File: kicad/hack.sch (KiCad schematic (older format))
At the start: 34 parts, among them P1 USB_micro, P2 CONN_01X13, P3 CONN_01X13, P4 CONN_01X01, U1 MIC5528, U2 STF202, U3 ATSAMD21E, X1 ABS07

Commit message: Added VBUS pin, GND pin near VDDANA
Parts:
- added P5, P6: CONN_01X01, hack-footprints:Pin_Castellated_1x01, symbol CONN_01X01
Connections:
- net GND: now also P6.1 (P1)
- net VBUS: now also P5.1 (P1)
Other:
- moved on the sheet: P4
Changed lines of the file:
@@
 Text GLabel 2825 6075 2    40   BiDi ~ 0
 PA16/6
-Text GLabel 2425 7275 3    40   Output ~ 0
+Text GLabel 2625 7275 3    40   Output ~ 0
 VDDANA
 $Comp
@@
 L CONN_01X01 P4
 U 1 1 568E26C4
-P 2425 7075
-F 0 "P4" V 2425 7175 40  0000 L CNB
-F 1 "CONN_01X01" V 2525 6900 40  0000 L CNB
-F 2 "hack-footprints:Pin_Castellated_1x01" H 2425 7075 50  0001 C CNN
-F 3 "" H 2425 7075 50  0000 C CNN
-	1    2425 7075
+P 2625 7075
+F 0 "P4" V 2625 7175 40  0000 L CNB
+F 1 "CONN_01X01" V 2725 6900 40  0000 L CNB
+F 2 "hack-footprints:Pin_Castellated_1x01" H 2625 7075 50  0001 C CNN
+F 3 "" H 2625 7075 50  0000 C CNN
+	1    2625 7075
 	0    -1   -1   0
 $EndComp
@@
 	1    0    0    -1
 $EndComp
+Text GLabel 2225 7275 3    40   Output ~ 0
+VBUS
+$Comp
+L CONN_01X01 P5
+U 1 1 569F6050
+P 2225 7075
+F 0 "P5" V 2225 7175 40  0000 L CNB
+F 1 "CONN_01X01" V 2325 6900 40  0000 L CNB
+F 2 "hack-footprints:Pin_Castellated_1x01" H 2225 7075 50  0001 C CNN
+F 3 "" H 2225 7075 50  0000 C CNN
+	1    2225 7075
+	0    -1   -1   0
+$EndComp
+Text GLabel 1825 7275 3    40   Output ~ 0
+GND
+$Comp
+L CONN_01X01 P6
+U 1 1 569F8542
+P 1825 7075
+F 0 "P6" V 1825 7175 40  0000 L CNB
+F 1 "CONN_01X01" V 1925 6900 40  0000 L CNB
+F 2 "hack-footprints:Pin_Castellated_1x01" H 1825 7075 50  0001 C CNN
+F 3 "" H 1825 7075 50  0000 C CNN
+	1    1825 7075
+	0    -1   -1   0
+$EndComp
 $EndSCHEMATC

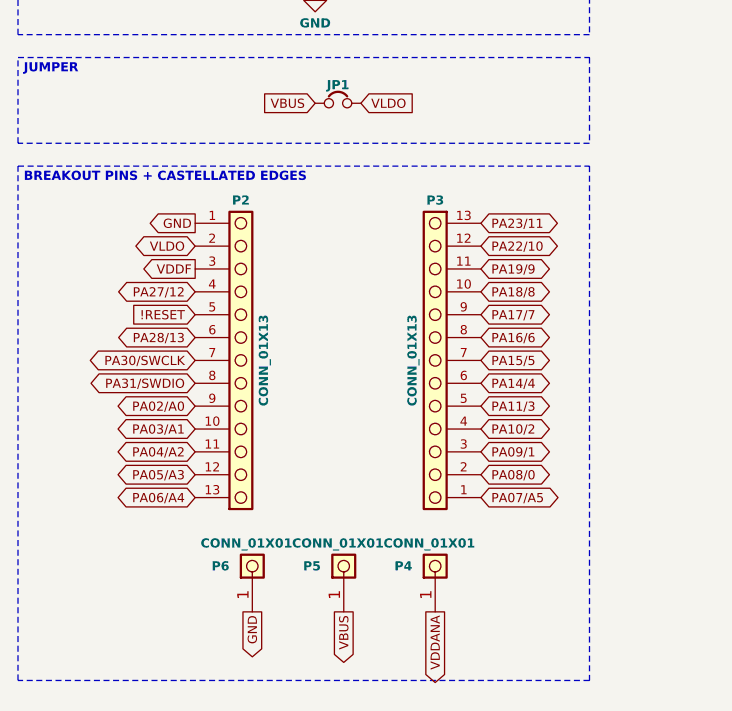
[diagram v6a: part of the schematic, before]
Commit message: Reducing board size (w.i.p.)
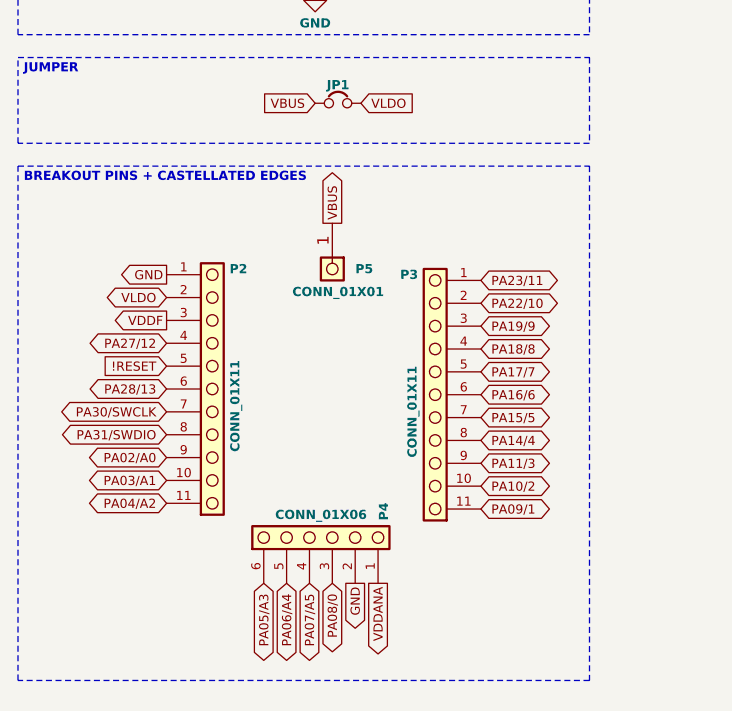
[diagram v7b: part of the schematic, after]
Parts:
- removed P2, P3: CONN_01X13, hack-footprints:Pin_Castellated_1x13, symbol CONN_01X13
- removed P4, P6: CONN_01X01, hack-footprints:Pin_Castellated_1x01, symbol CONN_01X01
- added P2, P3: CONN_01X11, hack-footprints:Pin_Castellated_1x11, symbol CONN_01X11
- added P4: CONN_01X06, hack-footprints:Pin_Castellated_1x06, symbol CONN_01X06
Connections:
- net !RESET: now also P2.5 (P5)
- net GND: now also P2.1 (P1), P4.2 (P2)
- net PA02/A0: now also P2.9 (P9)
- net PA03/A1: now also P2.10 (P10)
- net PA04/A2: now also P2.11 (P11)
- net PA05/A3: now also P4.6 (P6)
- net PA06/A4: now also P4.5 (P5)
- net PA07/A5: now also P4.4 (P4)
- net PA08/0: now also P4.3 (P3)
- net PA09/1: now also P3.11 (P11)
- net PA10/2: now also P3.10 (P10)
- net PA11/3: now also P3.9 (P9)
- net PA14/4: now also P3.8 (P8)
- net PA15/5: now also P3.7 (P7)
- net PA16/6: now also P3.6 (P6)
- net PA17/7: now also P3.5 (P5)
- net PA18/8: now also P3.4 (P4)
- net PA19/9: now also P3.3 (P3)
- net PA22/10: now also P3.2 (P2)
- net PA23/11: now also P3.1 (P1)
- net PA27/12: now also P2.4 (P4)
- net PA28/13: now also P2.6 (P6)
- net PA30/SWCLK: now also P2.7 (P7)
- net PA31/SWDIO: now also P2.8 (P8)
- net VDDANA: now also P4.1 (P1)
- net VDDF: now also P2.3 (P3)
- net VLDO: now also P2.2 (P2)
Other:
- moved on the sheet: P5
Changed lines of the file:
@@
-$EndComp
-$Comp
-L CONN_01X13 P2
-U 1 1 56587624
-P 1775 6175
-F 0 "P2" H 1775 6875 40  0000 C CNB
-F 1 "CONN_01X13" V 1875 6175 40  0000 C CNB
-F 2 "hack-footprints:Pin_Castellated_1x13" H 1775 6175 40  0001 C CNB
-F 3 "https://github.com/MickMad/HACK/tree/master/kicad/datasheets/xRxCzzzSxxN-RC_ST_11635-B.pdf" H 1775 6175 40  0001 C CNB
-F 4 "PREC014SACN-RC" H 1775 6175 60  0001 C CNN "manf#"
-	1    1775 6175
-	1    0    0    -1
 $EndComp
 $Comp
@@
 Text GLabel 2300 5050 2    40   Input ~ 0
 VLDO
-Text GLabel 1575 5575 0    40   Output ~ 0
+Text GLabel 1450 5800 0    40   Output ~ 0
 GND
-Text GLabel 1575 5675 0    40   BiDi ~ 0
+Text GLabel 1450 5900 0    40   BiDi ~ 0
 VLDO
-Text GLabel 1575 5775 0    40   Output ~ 0
+Text GLabel 1450 6000 0    40   Output ~ 0
 VDDF
-Text GLabel 2825 5975 2    40   BiDi ~ 0
+Text GLabel 2825 6225 2    40   BiDi ~ 0
 PA17/7
-Text GLabel 2825 5875 2    40   BiDi ~ 0
+Text GLabel 2825 6125 2    40   BiDi ~ 0
 PA18/8
-Text GLabel 2825 5775 2    40   BiDi ~ 0
+Text GLabel 2825 6025 2    40   BiDi ~ 0
 PA19/9
-Text GLabel 2825 5675 2    40   BiDi ~ 0
+Text GLabel 2825 5925 2    40   BiDi ~ 0
 PA22/10
-Text GLabel 2825 5575 2    40   BiDi ~ 0
+Text GLabel 2825 5825 2    40   BiDi ~ 0
 PA23/11
-Text GLabel 1575 5875 0    40   BiDi ~ 0
+Text GLabel 1450 6100 0    40   BiDi ~ 0
 PA27/12
-Text GLabel 1575 5975 0    40   Input ~ 0
+Text GLabel 1450 6200 0    40   Input ~ 0
 !RESET
-Text GLabel 1575 6075 0    40   BiDi ~ 0
+Text GLabel 1450 6300 0    40   BiDi ~ 0
 PA28/13
-Text GLabel 1575 6175 0    40   BiDi ~ 0
+Text GLabel 1450 6400 0    40   BiDi ~ 0
 PA30/SWCLK
-Text GLabel 1575 6275 0    40   BiDi ~ 0
+Text GLabel 1450 6500 0    40   BiDi ~ 0
 PA31/SWDIO
 Text GLabel 5700 1625 0    40   Input ~ 0
@@
 Text GLabel 2775 1400 2    40   Output ~ 0
 USB-D-
-Text GLabel 1575 6375 0    40   BiDi ~ 0
+Text GLabel 1450 6600 0    40   BiDi ~ 0
 PA02/A0
-Text GLabel 1575 6475 0    40   BiDi ~ 0
+Text GLabel 1450 6700 0    40   BiDi ~ 0
 PA03/A1
-Text GLabel 1575 6575 0    40   BiDi ~ 0
+Text GLabel 1450 6800 0    40   BiDi ~ 0
 PA04/A2
-Text GLabel 1575 6675 0    40   BiDi ~ 0
+Text GLabel 1875 7150 3    40   BiDi ~ 0
 PA05/A3
-Text GLabel 1575 6775 0    40   BiDi ~ 0
+Text GLabel 1975 7150 3    40   BiDi ~ 0
 PA06/A4
-Text GLabel 2825 6775 2    40   BiDi ~ 0
+Text GLabel 2075 7150 3    40   BiDi ~ 0
 PA07/A5
-Text GLabel 2825 6175 2    40   BiDi ~ 0
+Text GLabel 2825 6425 2    40   BiDi ~ 0
 PA15/5
-Text GLabel 2825 6275 2    40   BiDi ~ 0
+Text GLabel 2825 6525 2    40   BiDi ~ 0
 PA14/4
-Text GLabel 2825 6375 2    40   BiDi ~ 0
+Text GLabel 2825 6625 2    40   BiDi ~ 0
 PA11/3
-Text GLabel 2825 6475 2    40   BiDi ~ 0
+Text GLabel 2825 6725 2    40   BiDi ~ 0
 PA10/2
-Text GLabel 2825 6575 2    40   BiDi ~ 0
+Text GLabel 2825 6825 2    40   BiDi ~ 0
 PA09/1
-Text GLabel 2825 6675 2    40   BiDi ~ 0
+Text GLabel 2175 7150 3    40   BiDi ~ 0
 PA08/0
-Text GLabel 2825 6075 2    40   BiDi ~ 0
+Text GLabel 2825 6325 2    40   BiDi ~ 0
 PA16/6
-Text GLabel 2625 7275 3    40   Output ~ 0
+Text GLabel 2375 7150 3    40   Output ~ 0
 VDDANA
 $Comp
@@
 $EndComp
 $Comp
-L CONN_01X13 P3
-U 1 1 568E22DB
-P 2625 6175
-F 0 "P3" H 2625 5475 40  0000 C CNB
-F 1 "CONN_01X13" V 2725 6175 40  0000 C CNB
-F 2 "hack-footprints:Pin_Castellated_1x13" H 2625 6175 40  0001 C CNB
-F 3 "https://github.com/MickMad/HACK/tree/master/kicad/datasheets/320020128.pdf" H 2625 6175 40  0001 C CNB
-F 4 "PREC014SACN-RC" H 2625 6175 60  0001 C CNN "manf#"
-	1    2625 6175
-	-1   0    0    1
-$EndComp
-$Comp
-L CONN_01X01 P4
-U 1 1 568E26C4
-P 2625 7075
-F 0 "P4" V 2625 7175 40  0000 L CNB
-F 1 "CONN_01X01" V 2725 6900 40  0000 L CNB
-F 2 "hack-footprints:Pin_Castellated_1x01" H 2625 7075 50  0001 C CNN
-F 3 "" H 2625 7075 50  0000 C CNN
-	1    2625 7075
-	0    -1   -1   0
-$EndComp
-$Comp
 L ATSAMD21E U3
 U 1 1 568E2B7A
@@
 	1    0    0    -1
 $EndComp
-Text GLabel 2225 7275 3    40   Output ~ 0
+Text GLabel 2175 5575 1    40   Output ~ 0
 VBUS
 $Comp
 L CONN_01X01 P5
 U 1 1 569F6050
-P 2225 7075
-F 0 "P5" V 2225 7175 40  0000 L CNB
-F 1 "CONN_01X01" V 2325 6900 40  0000 L CNB
-F 2 "hack-footprints:Pin_Castellated_1x01" H 2225 7075 50  0001 C CNN
-F 3 "" H 2225 7075 50  0000 C CNN
-	1    2225 7075
-	0    -1   -1   0
-$EndComp
-Text GLabel 1825 7275 3    40   Output ~ 0
+P 2175 5775
+F 0 "P5" V 2175 5875 40  0000 L CNB
+F 1 "CONN_01X01" V 2275 5600 40  0000 L CNB
+F 2 "hack-footprints:Pin_Castellated_1x01" H 2175 5775 50  0001 C CNN
+F 3 "" H 2175 5775 50  0000 C CNN
+	1    2175 5775
+	0    1    1    0
+$EndComp
+Text GLabel 2275 7150 3    40   Output ~ 0
 GND
 $Comp
-L CONN_01X01 P6
-U 1 1 569F8542
-P 1825 7075
-F 0 "P6" V 1825 7175 40  0000 L CNB
-F 1 "CONN_01X01" V 1925 6900 40  0000 L CNB
-F 2 "hack-footprints:Pin_Castellated_1x01" H 1825 7075 50  0001 C CNN
-F 3 "" H 1825 7075 50  0000 C CNN
-	1    1825 7075
-	0    -1   -1   0
+L CONN_01X06 P4
+U 1 1 56A11B5B
+P 2125 6950
+F 0 "P4" H 2200 7225 40  0000 L CNB
+F 1 "CONN_01X06" V 2225 6750 40  0000 L CNB
+F 2 "hack-footprints:Pin_Castellated_1x06" H 2125 6600 50  0001 C CNN
+F 3 "" H 2125 6600 50  0000 C CNN
+	1    2125 6950
+	0    1    -1   0
+$EndComp
+$Comp
+L CONN_01X11 P2
+U 1 1 56A1367E
+P 1650 6300
+F 0 "P2" H 1725 6825 40  0000 L CNB
+F 1 "CONN_01X11" V 1750 6025 40  0000 L CNB
+F 2 "hack-footprints:Pin_Castellated_1x11" H 1650 6200 50  0001 C CNN
+F 3 "" H 1650 6200 50  0000 C CNN
+	1    1650 6300
+	1    0    0    -1
+$EndComp
+$Comp
+L CONN_01X11 P3
+U 1 1 56A13781
+P 2625 6325
+F 0 "P3" H 2700 6850 40  0000 L CNB
+F 1 "CONN_01X11" V 2725 6050 40  0000 L CNB
+F 2 "hack-footprints:Pin_Castellated_1x11" H 2625 6225 50  0001 C CNN
+F 3 "" H 2625 6225 50  0000 C CNN
+	1    2625 6325
+	-1   0    0    -1
 $EndComp
 $EndSCHEMATC

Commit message: Reduced overall board size
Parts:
- P4: manf# (none) -> 1
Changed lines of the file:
@@
 F 2 "hack-footprints:Pin_Castellated_1x06" H 2125 6600 50  0001 C CNN
 F 3 "" H 2125 6600 50  0000 C CNN
+F 4 "1" H 2125 6950 60  0001 C CNN "manf#"
 	1    2125 6950
 	0    1    -1   0
